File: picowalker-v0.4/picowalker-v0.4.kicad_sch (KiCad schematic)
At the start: 0 parts

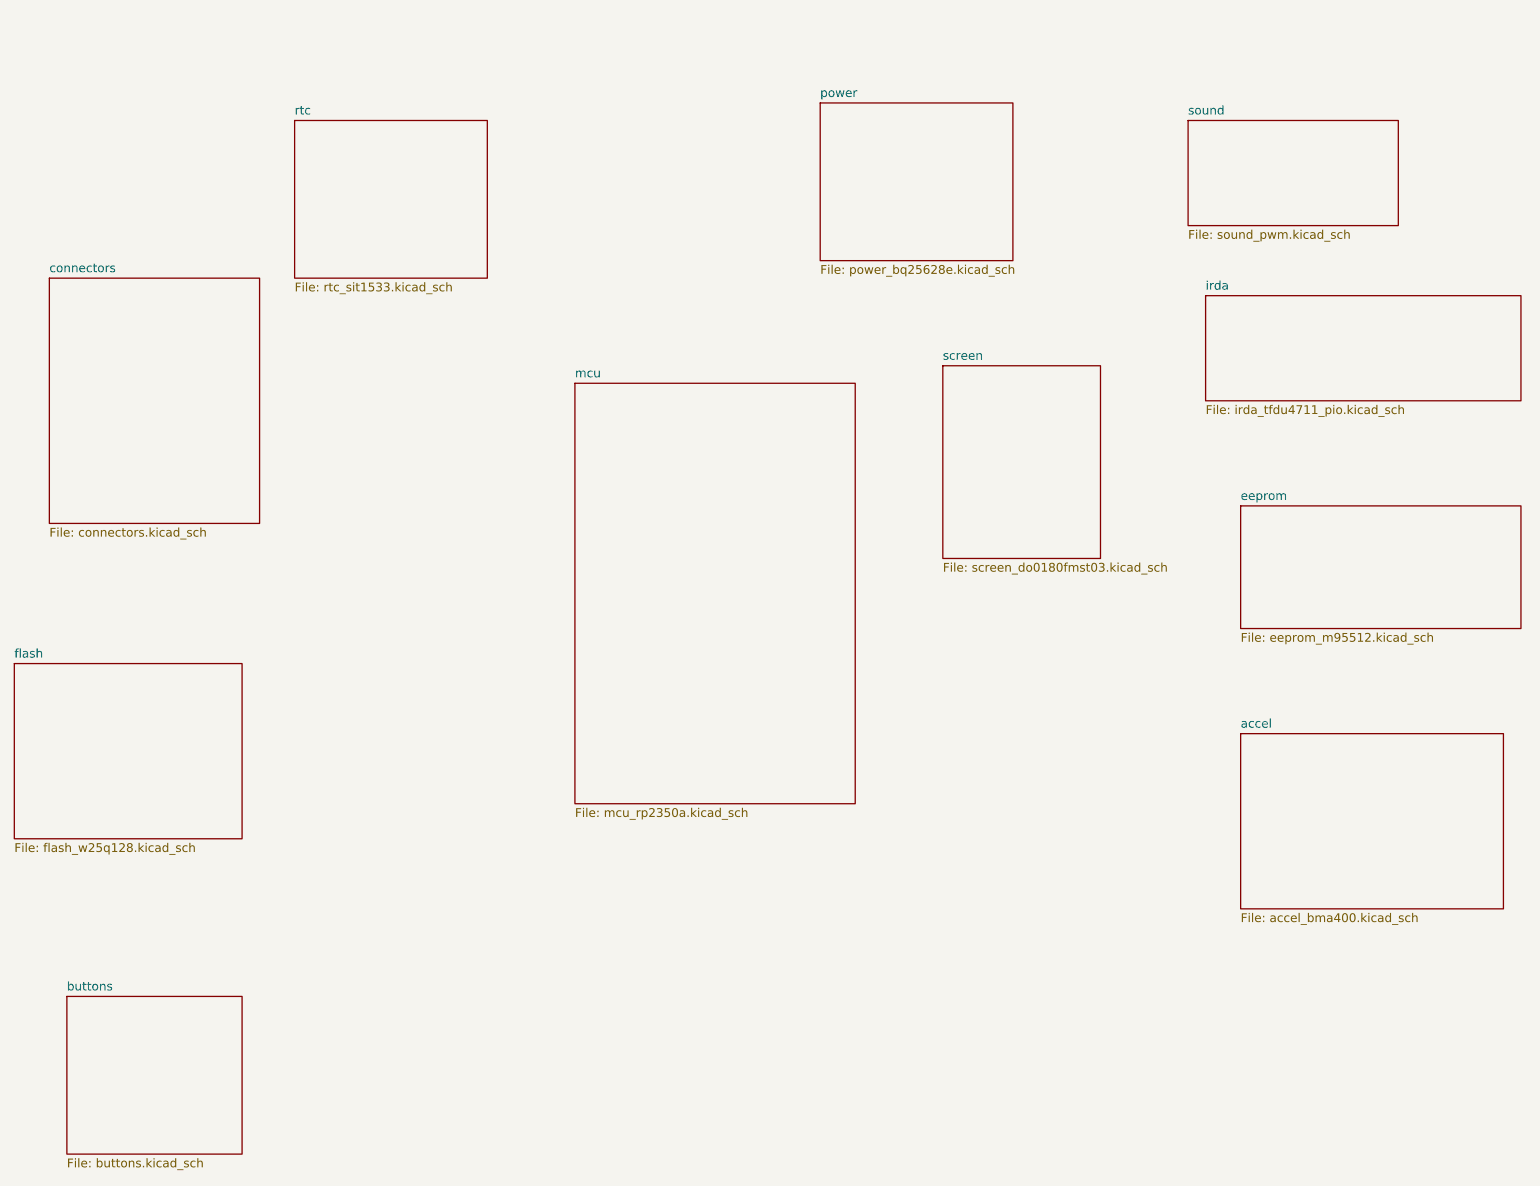
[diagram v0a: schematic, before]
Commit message: v0.4: schematic laid out first draft
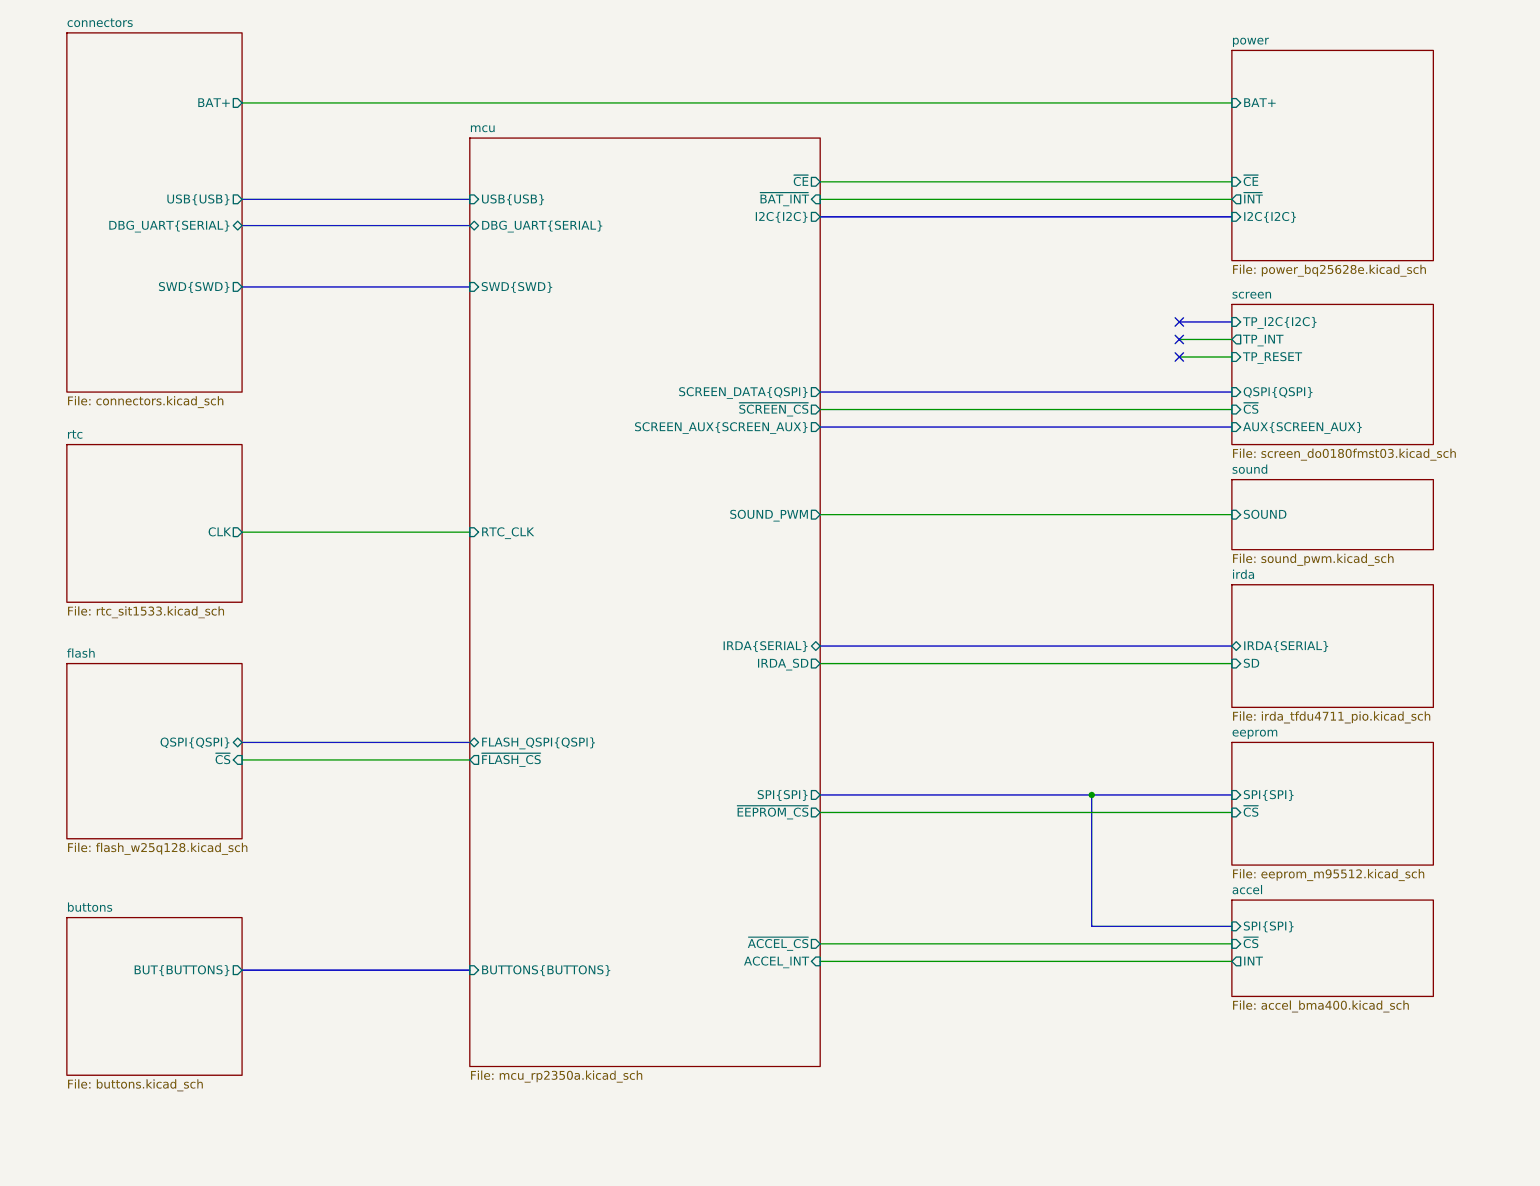
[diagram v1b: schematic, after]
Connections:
- no-connect marks 0 -> 3
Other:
- sheet accel ports: added INT, SPI{SPI}, ~{CS}; removed none
- sheet buttons ports: added BUT{BUTTONS}; removed none
- sheet connectors ports: added BAT+, DBG_UART{SERIAL}, SWD{SWD}, USB{USB}; removed none
- sheet eeprom ports: added SPI{SPI}, ~{CS}; removed none
- sheet flash ports: added QSPI{QSPI}, ~{CS}; removed none
- sheet irda ports: added IRDA{SERIAL}, SD; removed none
- sheet mcu ports: added ACCEL_INT, BUTTONS{BUTTONS}, DBG_UART{SERIAL}, FLASH_QSPI{QSPI}, I2C{I2C}, IRDA_SD, IRDA{SERIAL}, RTC_CLK, SCREEN_AUX{SCREEN_AUX}, SCREEN_DATA{QSPI}, SOUND_PWM, SPI{SPI}, SWD{SWD}, USB{USB}, ~{ACCEL_CS}, ~{BAT_INT}, ~{CE}, ~{EEPROM_CS}, ~{FLASH_CS}, ~{SCREEN_CS}; removed none
- sheet power ports: added BAT+, I2C{I2C}, ~{CE}, ~{INT}; removed none
- sheet rtc ports: added CLK; removed none
- sheet screen ports: added AUX{SCREEN_AUX}, QSPI{QSPI}, TP_I2C{I2C}, TP_INT, TP_RESET, ~{CS}; removed none
- sheet sound ports: added SOUND; removed none

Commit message: v0.4: good start on routing
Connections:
- no-connect marks 3 -> 4
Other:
- sheet screen ports: added TE; removed none
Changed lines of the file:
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@@
 	)
 	(bus_alias "I2C"
-		(members "SCK" "SDA")
+		(members "SCL" "SDA")
 	)
 	(bus_alias "QSPI"
@@
 	)
 	(no_connect
-		(at 201.93 64.77)
+		(at 194.31 64.77)
 	)
 	(no_connect
-		(at 201.93 67.31)
+		(at 194.31 67.31)
 	)
 	(no_connect
-		(at 201.93 62.23)
+		(at 194.31 69.85)
+	)
+	(no_connect
+		(at 194.31 62.23)
 	)
 	(bus
@@
 	(wire
 		(pts
+			(xy 194.31 67.31) (xy 209.55 67.31)
+		)
+		(stroke
+			(width 0)
+			(type default)
+		)
+	)
+	(wire
+		(pts
 			(xy 149.86 154.94) (xy 209.55 154.94)
 		)
@@
 	(wire
 		(pts
-			(xy 201.93 64.77) (xy 209.55 64.77)
-		)
-		(stroke
-			(width 0)
-			(type default)
-		)
-	)
-	(wire
-		(pts
 			(xy 66.04 30.48) (xy 209.55 30.48)
 		)
@@
 	(wire
 		(pts
-			(xy 201.93 67.31) (xy 209.55 67.31)
-		)
-		(stroke
-			(width 0)
-			(type default)
-		)
-	)
-	(wire
-		(pts
 			(xy 149.86 44.45) (xy 209.55 44.45)
 		)
@@
 	(bus
 		(pts
-			(xy 201.93 62.23) (xy 209.55 62.23)
-		)
-		(stroke
-			(width 0)
-			(type default)
-		)
-	)
-	(bus
-		(pts
 			(xy 149.86 72.39) (xy 209.55 72.39)
 		)
@@
 	(wire
 		(pts
+			(xy 194.31 64.77) (xy 209.55 64.77)
+		)
+		(stroke
+			(width 0)
+			(type default)
+		)
+	)
+	(wire
+		(pts
 			(xy 149.86 133.35) (xy 209.55 133.35)
 		)
@@
 		)
 	)
+	(wire
+		(pts
+			(xy 194.31 69.85) (xy 209.55 69.85)
+		)
+		(stroke
+			(width 0)
+			(type default)
+		)
+	)
+	(bus
+		(pts
+			(xy 194.31 62.23) (xy 209.55 62.23)
+		)
+		(stroke
+			(width 0)
+			(type default)
+		)
+	)
 	(bus
 		(pts
@@
 			(width 0)
 			(type default)
+		)
+	)
+	(label "SOUND"
+		(at 177.8 90.17 0)
+		(effects
+			(font
+				(size 1.27 1.27)
+			)
+			(justify left bottom)
+		)
+	)
+	(label "~{BAT_CE}"
+		(at 173.99 41.91 0)
+		(effects
+			(font
+				(size 1.27 1.27)
+			)
+			(justify left bottom)
+		)
+	)
+	(label "~{BAT_INT}"
+		(at 173.99 44.45 0)
+		(effects
+			(font
+				(size 1.27 1.27)
+			)
+			(justify left bottom)
+		)
+	)
+	(label "~{ACCEL_CS}"
+		(at 175.26 152.4 0)
+		(effects
+			(font
+				(size 1.27 1.27)
+			)
+			(justify left bottom)
+		)
+	)
+	(label "IRDA_SD"
+		(at 176.53 111.76 0)
+		(effects
+			(font
+				(size 1.27 1.27)
+			)
+			(justify left bottom)
+		)
+	)
+	(label "~{SCREEN_CS}"
+		(at 175.26 74.93 0)
+		(effects
+			(font
+				(size 1.27 1.27)
+			)
+			(justify left bottom)
+		)
+	)
+	(label "~{EEPROM_CS}"
+		(at 175.26 133.35 0)
+		(effects
+			(font
+				(size 1.27 1.27)
+			)
+			(justify left bottom)
+		)
+	)
+	(label "ACCEL_INT"
+		(at 175.26 154.94 0)
+		(effects
+			(font
+				(size 1.27 1.27)
+			)
+			(justify left bottom)
 		)
 	)
@@
 		)
 		(pin "TP_INT" output
+			(at 209.55 67.31 180)
+			(effects
+				(font
+					(size 1.27 1.27)
+				)
+				(justify left)
+			)
+		)
+		(pin "TP_RESET" input
 			(at 209.55 64.77 180)
 			(effects
@@
 			)
 		)
-		(pin "TP_RESET" input
-			(at 209.55 67.31 180)
-			(effects
-				(font
+		(pin "TE" output
+			(at 209.55 69.85 180)
+			(effects
+				(font

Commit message: v0.4: running DRC checks
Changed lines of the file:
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@@
+		)
+	)
+	(label "TP_INT"
+		(at 199.39 67.31 0)
+		(effects
+			(font
+				(size 1.27 1.27)
+			)
+			(justify left bottom)
 		)
 	)
@@
 		(effects
 			(font
+				(size 1.27 1.27)
+			)
+			(justify left bottom)
+		)
+	)
+	(label "TP_RESET"
+		(at 199.39 64.77 0)
+		(effects
+			(font
+				(size 1.27 1.27)
+			)
+			(justify left bottom)
+		)
+	)
+	(label "TE"
+		(at 199.39 69.85 0)
+		(effects
+			(font

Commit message: v0.4: add huawei speaker
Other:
- title: (none) -> picowalker
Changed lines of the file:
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@@
 	(generator_version "9.0")
 	(paper "A4")
+	(title_block
+		(title "picowalker")
+		(rev "0.4")
+	)
 	(bus_alias "BUTTONS"
 		(members "L" "M" "R")

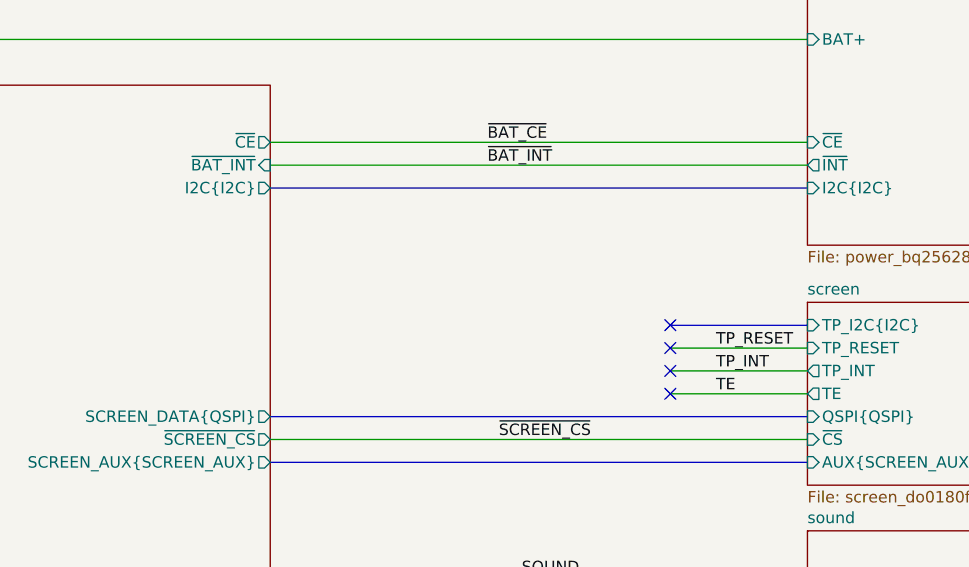
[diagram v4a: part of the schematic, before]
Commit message: v0.4: connect i2c to TP and add silkscreen labels
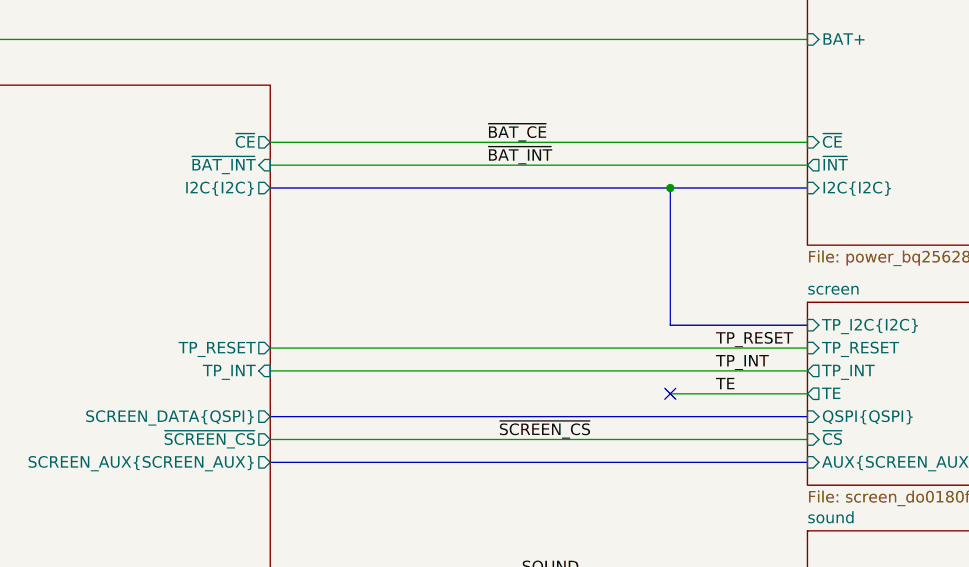
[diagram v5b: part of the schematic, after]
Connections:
- no-connect marks 4 -> 1
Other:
- sheet mcu ports: added TP_INT, TP_RESET; removed none
